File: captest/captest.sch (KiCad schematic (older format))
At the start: 12 parts, among them IC1 ATTINY861-P, P1 CONN_2, P2 CONN_6, P3 CONN_3X2

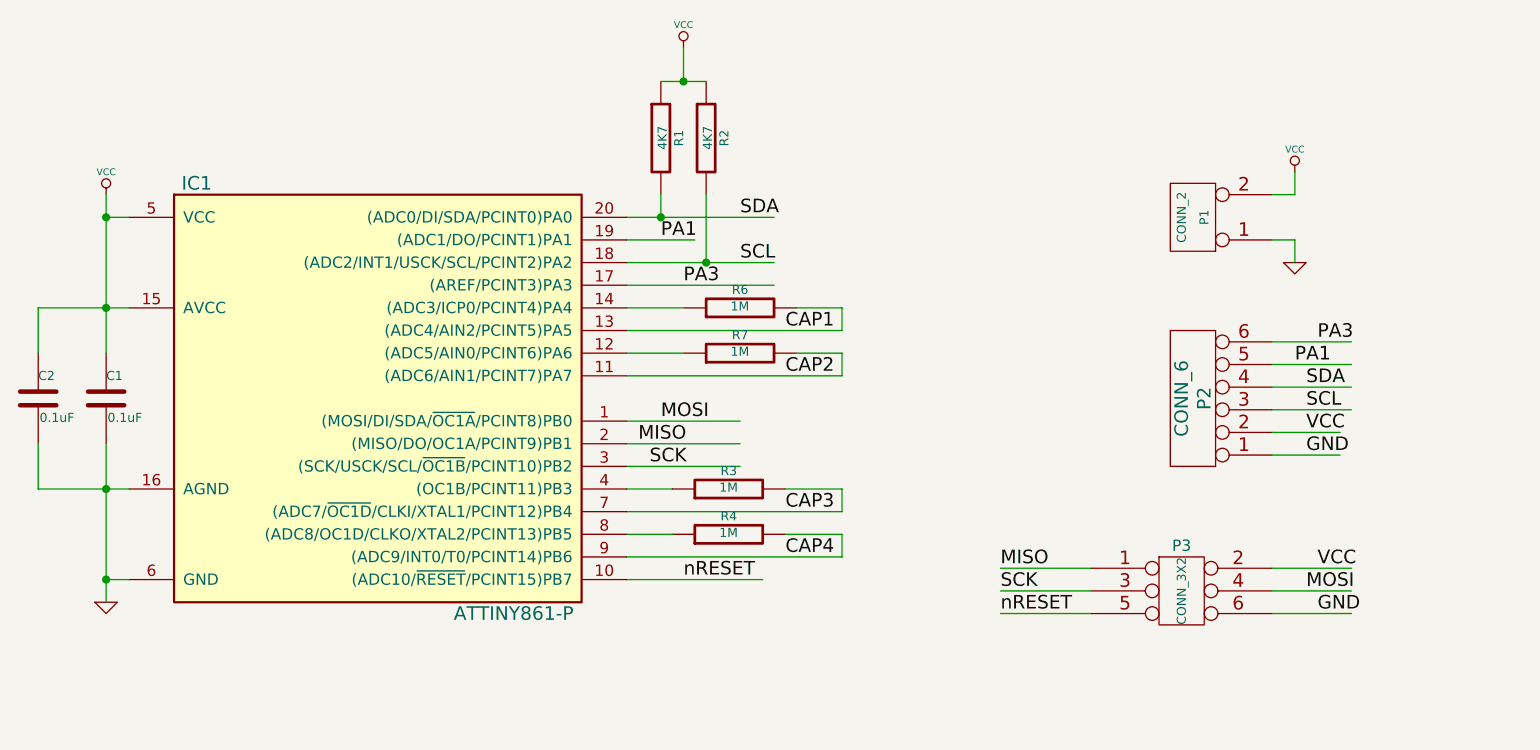
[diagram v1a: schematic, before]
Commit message: Captest updates
* Change to SOIC-20 version of ATtiny861
* Add filtering caps on sense pins
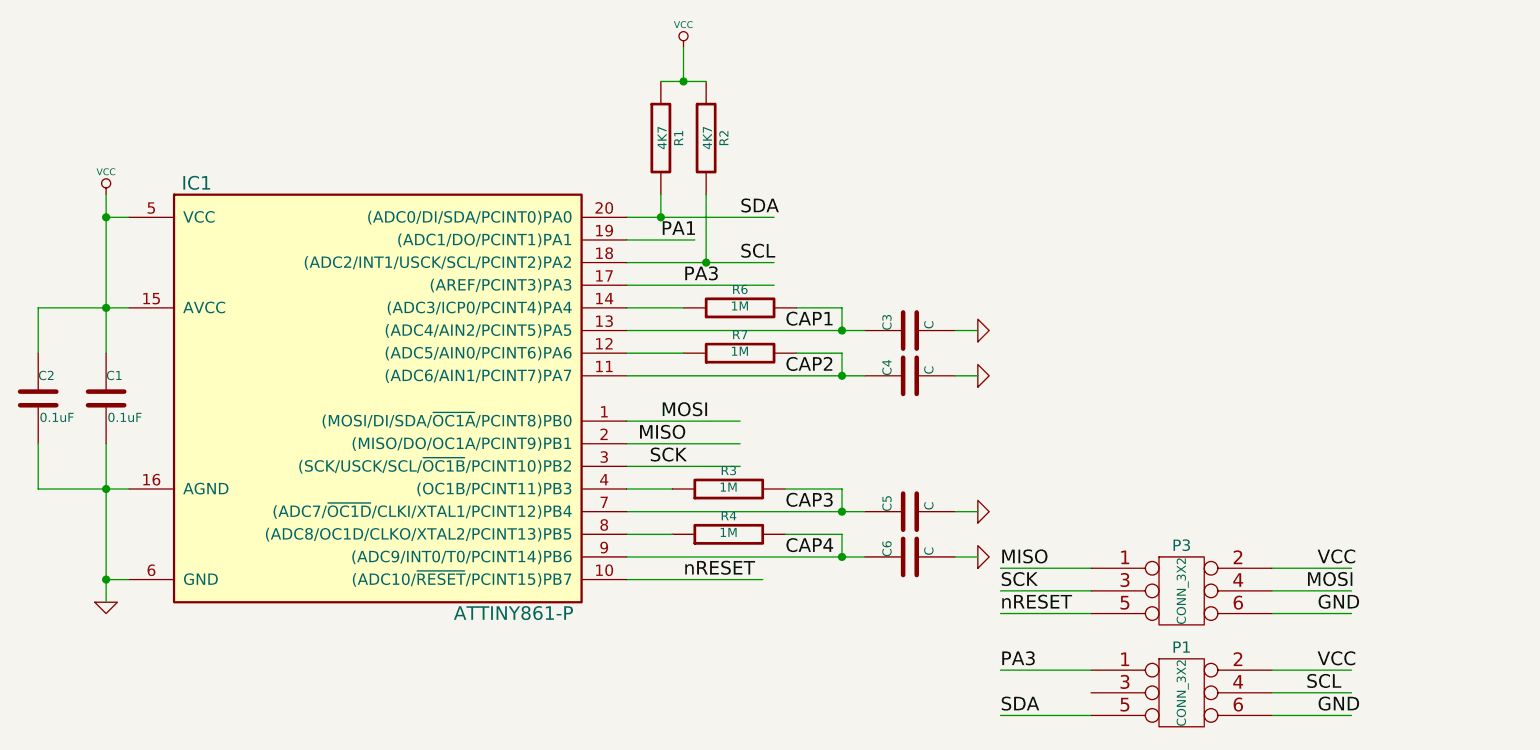
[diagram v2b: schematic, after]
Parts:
- removed P1: CONN_2, symbol CONN_2
- removed P2: CONN_6, symbol CONN_6
- added C3, C4, C5, C6: C, ~, symbol C
- added P1: CONN_3X2, symbol CONN_3X2
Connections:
- wire segments 52 -> 51
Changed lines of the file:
@@
-EESchema Schematic File Version 2  date Mon 04 Mar 2013 04:06:09 PM EST
+EESchema Schematic File Version 2  date Mon 04 Mar 2013 06:34:23 PM EST
 LIBS:power
 LIBS:device
@@
 	6800 2500 7050 2500
 Wire Wire Line
-	6800 2600 7750 2600
+	6800 2600 7850 2600
 Wire Wire Line
 	7750 2600 7750 2500
@@
 	6800 2700 7050 2700
 Wire Wire Line
-	6800 2800 7750 2800
+	6800 2800 7850 2800
 Wire Wire Line
 	7750 2800 7750 2700
@@
 Connection ~ 7050 1500
 Wire Wire Line
-	6800 3600 7750 3600
+	6800 3600 7850 3600
 Wire Wire Line
 	6800 3700 7400 3700
 Text Label 7050 3700 0    60   ~ 0
 nRESET
-$Comp
-L CONN_2 P1
-U 1 1 512E7DD4
-P 9300 2100
-F 0 "P1" V 9250 2100 40  0000 C CNN
-F 1 "CONN_2" V 9350 2100 40  0000 C CNN
-F 2 "" H 9300 2100 60  0000 C CNN
-F 3 "" H 9300 2100 60  0000 C CNN
-	1    9300 2100
-	-1   0    0    1
-$EndComp
-$Comp
-L GND #PWR03
-U 1 1 512E7DED
-P 9750 2300
-F 0 "#PWR03" H 9750 2300 30  0001 C CNN
-F 1 "GND" H 9750 2230 30  0001 C CNN
-F 2 "" H 9750 2300 60  0000 C CNN
-F 3 "" H 9750 2300 60  0000 C CNN
-	1    9750 2300
-	1    0    0    -1
-$EndComp
-Wire Wire Line
-	9650 2200 9750 2200
-Wire Wire Line
-	9750 2200 9750 2300
-$Comp
-L VCC #PWR04
-U 1 1 512E7E27
-P 9750 1900
-F 0 "#PWR04" H 9750 2000 30  0001 C CNN
-F 1 "VCC" H 9750 2000 30  0000 C CNN
-F 2 "" H 9750 1900 60  0000 C CNN
-F 3 "" H 9750 1900 60  0000 C CNN
-	1    9750 1900
-	1    0    0    -1
-$EndComp
-Wire Wire Line
-	9650 2000 9750 2000
-Wire Wire Line
-	9750 2000 9750 1900
-Wire Wire Line
-	9650 2950 10000 2950
-Text Label 9800 2950 0    60   ~ 0
-SCL
-Wire Wire Line
-	9650 2850 10000 2850
-Text Label 9800 2850 0    60   ~ 0
-SDA
 Wire Wire Line
 	6800 2200 7100 2200
 Text Label 6950 2200 0    60   ~ 0
 PA1
-$Comp
-L CONN_6 P2
-U 1 1 512E8037
-P 9300 2900
-F 0 "P2" V 9250 2900 60  0000 C CNN
-F 1 "CONN_6" V 9350 2900 60  0000 C CNN
-F 2 "" H 9300 2900 60  0000 C CNN
-F 3 "" H 9300 2900 60  0000 C CNN
-	1    9300 2900
-	-1   0    0    1
-$EndComp
-Wire Wire Line
-	9650 2650 10000 2650
-Text Label 9850 2650 0    60   ~ 0
-PA3
-Wire Wire Line
-	9650 3050 9950 3050
-Text Label 9800 3050 0    60   ~ 0
-VCC
-Wire Wire Line
-	9650 3150 9950 3150
-Text Label 9800 3150 0    60   ~ 0
-GND
 $Comp
 L ATTINY861-P IC1
@@
 	6800 3200 7300 3200
 Wire Wire Line
-	9650 2750 10000 2750
-Wire Wire Line
 	6800 2400 7450 2400
-Text Label 9750 2750 0    60   ~ 0
-PA1
 $Comp
 L R R3
@@
 	6800 3500 7000 3500
 Wire Wire Line
-	6800 3400 7750 3400
+	6800 3400 7850 3400
 Wire Wire Line
 	7750 3400 7750 3300
@@
 PA3
 $Comp
-L VCC #PWR05
+L VCC #PWR03
 U 1 1 513508A4
 P 4500 2000
-F 0 "#PWR05" H 4500 2100 30  0001 C CNN
+F 0 "#PWR03" H 4500 2100 30  0001 C CNN
 F 1 "VCC" H 4500 2100 30  0000 C CNN
 F 2 "" H 4500 2000 60  0000 C CNN
@@
 $EndComp
 Connection ~ 4500 2100
+$Comp
+L C C3
+U 1 1 51352673
+P 8050 2600
+F 0 "C3" H 8050 2700 40  0000 L CNN
+F 1 "C" H 8056 2515 40  0000 L CNN
+F 2 "~" H 8088 2450 30  0000 C CNN
+F 3 "~" H 8050 2600 60  0000 C CNN
+	1    8050 2600
+	0    -1   -1   0
+$EndComp
+$Comp
+L C C4
+U 1 1 51352682
+P 8050 2800
+F 0 "C4" H 8050 2900 40  0000 L CNN
+F 1 "C" H 8056 2715 40  0000 L CNN
+F 2 "~" H 8088 2650 30  0000 C CNN
+F 3 "~" H 8050 2800 60  0000 C CNN
+	1    8050 2800
+	0    -1   -1   0
+$EndComp
+Connection ~ 7750 2600
+Connection ~ 7750 2800
+$Comp
+L GND #PWR04
+U 1 1 5135270A
+P 8350 2600
+F 0 "#PWR04" H 8350 2600 30  0001 C CNN
+F 1 "GND" H 8350 2530 30  0001 C CNN
+F 2 "" H 8350 2600 60  0000 C CNN
+F 3 "" H 8350 2600 60  0000 C CNN
+	1    8350 2600
+	0    -1   -1   0
+$EndComp
+Wire Wire Line
+	8350 2600 8250 2600
+Wire Wire Line
+	8250 2800 8350 2800
+$Comp
+L GND #PWR05
+U 1 1 51352797
+P 8350 2800
+F 0 "#PWR05" H 8350 2800 30  0001 C CNN
+F 1 "GND" H 8350 2730 30  0001 C CNN
+F 2 "" H 8350 2800 60  0000 C CNN
+F 3 "" H 8350 2800 60  0000 C CNN
+	1    8350 2800
+	0    -1   -1   0
+$EndComp
+$Comp
+L C C5
+U 1 1 51352823
+P 8050 3400
+F 0 "C5" H 8050 3500 40  0000 L CNN
+F 1 "C" H 8056 3315 40  0000 L CNN
+F 2 "~" H 8088 3250 30  0000 C CNN
+F 3 "~" H 8050 3400 60  0000 C CNN
+	1    8050 3400
+	0    -1   -1   0
+$EndComp
+Connection ~ 7750 3400
+$Comp
+L GND #PWR06
+U 1 1 513528B2
+P 8350 3400
+F 0 "#PWR06" H 8350 3400 30  0001 C CNN
+F 1 "GND" H 8350 3330 30  0001 C CNN
+F 2 "" H 8350 3400 60  0000 C CNN
+F 3 "" H 8350 3400 60  0000 C CNN
+	1    8350 3400
+	0    -1   -1   0
+$EndComp
+Wire Wire Line
+	8350 3400 8250 3400
+$Comp
+L C C6
+U 1 1 51352902
+P 8050 3600
+F 0 "C6" H 8050 3700 40  0000 L CNN
+F 1 "C" H 8056 3515 40  0000 L CNN
+F 2 "~" H 8088 3450 30  0000 C CNN
+F 3 "~" H 8050 3600 60  0000 C CNN
+	1    8050 3600
+	0    -1   -1   0
+$EndComp
+Connection ~ 7750 3600
+$Comp
+L GND #PWR07
+U 1 1 51352953
+P 8350 3600
+F 0 "#PWR07" H 8350 3600 30  0001 C CNN
+F 1 "GND" H 8350 3530 30  0001 C CNN
+F 2 "" H 8350 3600 60  0000 C CNN
+F 3 "" H 8350 3600 60  0000 C CNN
+	1    8350 3600
+	0    -1   -1   0
+$EndComp
+Wire Wire Line
+	8350 3600 8250 3600
+$Comp
+L CONN_3X2 P1
+U 1 1 513529F0
+P 9250 4250
+F 0 "P1" H 9250 4500 50  0000 C CNN
+F 1 "CONN_3X2" V 9250 4300 40  0000 C CNN
+F 2 "" H 9250 4250 60  0000 C CNN
+F 3 "" H 9250 4250 60  0000 C CNN
+	1    9250 4250
+	1    0    0    -1
+$EndComp
+Wire Wire Line
+	9650 4100 10000 4100
+Wire Wire Line
+	9650 4200 10000 4200
+Wire Wire Line
+	9650 4300 10000 4300
+Wire Wire Line
+	8450 4100 8850 4100
+Wire Wire Line
+	8450 4300 8850 4300
+Text Label 9850 4100 0    60   ~ 0
+VCC
+Text Label 9800 4200 0    60   ~ 0
+SCL
+Text Label 9850 4300 0    60   ~ 0
+GND
+Text Label 8450 4100 0    60   ~ 0
+PA3
+Text Label 8450 4300 0    60   ~ 0
+SDA
 $EndSCHEMATC

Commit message: Captest update with TSSOP and more density
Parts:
- removed P3: CONN_3X2, symbol CONN_3X2
- added L1: INDUCTOR, ~, symbol INDUCTOR
- added P2: CONN_4, symbol CONN_4
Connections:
- net labels added: PWR
- net labels removed: PA1
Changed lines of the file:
@@
-EESchema Schematic File Version 2  date Mon 04 Mar 2013 06:34:23 PM EST
+EESchema Schematic File Version 2  date Tue 05 Mar 2013 12:00:50 PM EST
 LIBS:power
 LIBS:device
@@
 Sheet 1 1
 Title ""
-Date "4 mar 2013"
+Date "5 mar 2013"
 Rev ""
 Comp ""
@@
 	0    -1   -1   0
 $EndComp
-Wire Wire Line
-	6800 2500 7050 2500
-Wire Wire Line
-	6800 2600 7850 2600
-Wire Wire Line
-	7750 2600 7750 2500
-Wire Wire Line
-	7750 2500 7550 2500
-Wire Wire Line
-	6800 2700 7050 2700
-Wire Wire Line
-	6800 2800 7850 2800
-Wire Wire Line
-	7750 2800 7750 2700
-Wire Wire Line
-	7750 2700 7550 2700
 Text Label 7500 2800 0    60   ~ 0
 CAP2
 Text Label 7500 2600 0    60   ~ 0
 CAP1
-Wire Wire Line
-	6800 2100 7450 2100
-Wire Wire Line
-	6800 2300 7450 2300
 Text Label 7300 2300 0    60   ~ 0
 SCL
 Text Label 7300 2100 0    60   ~ 0
 SDA
-Wire Wire Line
-	4600 2100 4500 2100
-Wire Wire Line
-	4500 2000 4500 2700
-Wire Wire Line
-	4200 2500 4600 2500
 $Comp
 L GND #PWR01
@@
 	1    0    0    -1
 $EndComp
-Wire Wire Line
-	4500 3100 4500 3800
-Wire Wire Line
-	4500 3700 4600 3700
-Wire Wire Line
-	4200 3300 4600 3300
-Connection ~ 4500 3700
 $Comp
 L C C1
@@
 	1    0    0    -1
 $EndComp
-Connection ~ 4500 2500
-Connection ~ 4500 3300
 Text Label 6850 3100 0    60   ~ 0
 MISO
-Wire Wire Line
-	6800 3000 7300 3000
 Text Label 6950 3000 0    60   ~ 0
 MOSI
@@
 	1    0    0    -1
 $EndComp
-Wire Wire Line
-	7150 2000 7150 2300
-Connection ~ 7150 2300
-Wire Wire Line
-	6950 2000 6950 2100
-Connection ~ 6950 2100
 $Comp
 L VCC #PWR02
@@
 	1    0    0    -1
 $EndComp
-Wire Wire Line
-	6950 1500 7150 1500
-Wire Wire Line
-	7050 1500 7050 1350
-Connection ~ 7050 1500
-Wire Wire Line
-	6800 3600 7850 3600
-Wire Wire Line
-	6800 3700 7400 3700
 Text Label 7050 3700 0    60   ~ 0
 nRESET
-Wire Wire Line
-	6800 2200 7100 2200
-Text Label 6950 2200 0    60   ~ 0
-PA1
 $Comp
 L ATTINY861-P IC1
@@
 	1    0    0    -1
 $EndComp
-Wire Wire Line
-	6800 3100 7300 3100
-Wire Wire Line
-	6800 3200 7300 3200
-Wire Wire Line
-	6800 2400 7450 2400
 $Comp
 L R R3
@@
 	0    -1   -1   0
 $EndComp
-Wire Wire Line
-	6800 3300 7000 3300
 $Comp
 L R R4
@@
 	0    -1   -1   0
 $EndComp
-Wire Wire Line
-	6800 3500 7000 3500
-Wire Wire Line
-	6800 3400 7850 3400
-Wire Wire Line
-	7750 3400 7750 3300
-Wire Wire Line
-	7750 3300 7500 3300
-Wire Wire Line
-	7750 3600 7750 3500
-Wire Wire Line
-	7750 3500 7500 3500
 Text Label 7500 3400 0    60   ~ 0
 CAP3
 Text Label 7500 3600 0    60   ~ 0
 CAP4
-$Comp
-L CONN_3X2 P3
-U 1 1 5135027D
-P 9250 3800
-F 0 "P3" H 9250 4050 50  0000 C CNN
-F 1 "CONN_3X2" V 9250 3850 40  0000 C CNN
-F 2 "" H 9250 3800 60  0000 C CNN
-F 3 "" H 9250 3800 60  0000 C CNN
-	1    9250 3800
-	1    0    0    -1
-$EndComp
-Wire Wire Line
-	9650 3650 10000 3650
-Wire Wire Line
-	9650 3750 10000 3750
-Wire Wire Line
-	9650 3850 10000 3850
-Wire Wire Line
-	8450 3650 8850 3650
-Wire Wire Line
-	8450 3750 8850 3750
-Wire Wire Line
-	8450 3850 8850 3850
-Text Label 9850 3650 0    60   ~ 0
-VCC
-Text Label 9800 3750 0    60   ~ 0
-MOSI
-Text Label 9850 3850 0    60   ~ 0
-GND
 Text Label 8450 3650 0    60   ~ 0
 MISO
@@
 	1    0    0    -1
 $EndComp
-Wire Wire Line
-	4200 2700 4200 2500
-Wire Wire Line
-	4200 3100 4200 3300
 Text Label 7050 2400 0    60   ~ 0
 PA3
@@
 	1    0    0    -1
 $EndComp
-Connection ~ 4500 2100
 $Comp
 L C C3
@@
 	0    -1   -1   0
 $EndComp
-Connection ~ 7750 2600
-Connection ~ 7750 2800
 $Comp
 L GND #PWR04
@@
 	0    -1   -1   0
 $EndComp
-Wire Wire Line
-	8350 2600 8250 2600
-Wire Wire Line
-	8250 2800 8350 2800
 $Comp
 L GND #PWR05
@@
 	0    -1   -1   0
 $EndComp
-Connection ~ 7750 3400
 $Comp
 L GND #PWR06
@@
 	0    -1   -1   0
 $EndComp
-Wire Wire Line
-	8350 3400 8250 3400
 $Comp
 L C C6
@@
 	0    -1   -1   0
 $EndComp
-Connection ~ 7750 3600
 $Comp
 L GND #PWR07
@@
 	0    -1   -1   0
 $EndComp
-Wire Wire Line
-	8350 3600 8250 3600
 $Comp
 L CONN_3X2 P1
@@
 	1    0    0    -1
 $EndComp
-Wire Wire Line
-	9650 4100 10000 4100
-Wire Wire Line
-	9650 4200 10000 4200
-Wire Wire Line
-	9650 4300 10000 4300
-Wire Wire Line
-	8450 4100 8850 4100
-Wire Wire Line
-	8450 4300 8850 4300
-Text Label 9850 4100 0    60   ~ 0
-VCC
-Text Label 9800 4200 0    60   ~ 0
-SCL
 Text Label 9850 4300 0    60   ~ 0
 GND
 Text Label 8450 4100 0    60   ~ 0
+SDA
+Text Label 8450 4300 0    60   ~ 0
 PA3
-Text Label 8450 4300 0    60   ~ 0
+$Comp
+L INDUCTOR L1
+U 1 1 5136118C
+P 10300 4100
+F 0 "L1" V 10250 4100 40  0000 C CNN
+F 1 "INDUCTOR" V 10400 4100 40  0000 C CNN
+F 2 "~" H 10300 4100 60  0000 C CNN
+F 3 "~" H 10300 4100 60  0000 C CNN
+	1    10300 4100
+	0    -1   -1   0
+$EndComp
+Wire Wire Line
+	6800 2500 7050 2500
+Wire Wire Line
+	6800 2600 7850 2600
+Wire Wire Line
+	7750 2600 7750 2500
+Wire Wire Line
+	7750 2500 7550 2500
+Wire Wire Line
+	6800 2700 7050 2700
+Wire Wire Line
+	6800 2800 7850 2800
+Wire Wire Line
+	7750 2800 7750 2700
+Wire Wire Line
+	7750 2700 7550 2700
+Wire Wire Line
+	6800 2100 7450 2100
+Wire Wire Line
+	6800 2300 7450 2300
+Wire Wire Line
+	4600 2100 4500 2100
+Wire Wire Line
+	4500 2000 4500 2700
+Wire Wire Line
+	4200 2500 4600 2500
+Wire Wire Line
+	4500 3100 4500 3800
+Wire Wire Line
+	4500 3700 4600 3700
+Wire Wire Line
+	4200 3300 4600 3300
+Connection ~ 4500 3700
+Connection ~ 4500 2500
+Connection ~ 4500 3300
+Wire Wire Line
+	6800 3000 7300 3000
+Wire Wire Line
+	7150 2000 7150 2300
+Connection ~ 7150 2300
+Wire Wire Line
+	6950 2000 6950 2100
+Connection ~ 6950 2100
+Wire Wire Line
+	6950 1500 7150 1500
+Wire Wire Line
+	7050 1500 7050 1350
+Connection ~ 7050 1500
+Wire Wire Line
+	6800 3600 7850 3600
+Wire Wire Line
+	6800 3700 7400 3700
+Wire Wire Line
+	6800 3100 7300 3100
+Wire Wire Line
+	6800 3200 7300 3200
+Wire Wire Line
+	6800 2400 7450 2400
+Wire Wire Line
+	6800 3300 7000 3300
+Wire Wire Line
+	6800 3500 7000 3500
+Wire Wire Line
+	6800 3400 7850 3400
+Wire Wire Line
+	7750 3400 7750 3300
+Wire Wire Line
+	7750 3300 7500 3300
+Wire Wire Line
+	7750 3600 7750 3500
+Wire Wire Line
+	7750 3500 7500 3500
+Wire Wire Line
+	8450 3650 8850 3650
+Wire Wire Line
+	8450 3750 8850 3750
+Wire Wire Line
+	8450 3850 8850 3850
+Wire Wire Line
+	4200 2700 4200 2500
+Wire Wire Line
+	4200 3100 4200 3300
+Connection ~ 4500 2100
+Connection ~ 7750 2600
+Connection ~ 7750 2800
+Wire Wire Line
+	8350 2600 8250 2600
+Wire Wire Line
+	8250 2800 8350 2800
+Connection ~ 7750 3400
+Wire Wire Line
+	8350 3400 8250 3400
+Connection ~ 7750 3600
+Wire Wire Line
+	8350 3600 8250 3600
+Wire Wire Line
+	9650 4100 10000 4100
+Wire Wire Line
+	9650 4200 10000 4200
+Wire Wire Line
+	9650 4300 10000 4300
+Wire Wire Line
+	8450 4100 8850 4100
+Wire Wire Line
+	8450 4300 8850 4300
+$Comp
+L VCC #PWR08
+U 1 1 51361A88
+P 10700 4000
+F 0 "#PWR08" H 10700 4100 30  0001 C CNN
+F 1 "VCC" H 10700 4100 30  0000 C CNN
+F 2 "" H 10700 4000 60  0000 C CNN
+F 3 "" H 10700 4000 60  0000 C CNN
+	1    10700 4000
+	1    0    0    -1
+$EndComp
+Wire Wire Line
+	10700 4000 10700 4100
+Wire Wire Line
+	10700 4100 10600 4100
+$Comp
+L CONN_4 P2
+U 1 1 51361ADF
+P 9200 3700
+F 0 "P2" V 9150 3700 50  0000 C CNN
+F 1 "CONN_4" V 9250 3700 50  0000 C CNN
+F 2 "" H 9200 3700 60  0000 C CNN
+F 3 "" H 9200 3700 60  0000 C CNN
+	1    9200 3700
+	1    0    0    -1
+$EndComp
+Wire Wire Line
+	8850 3550 8450 3550
+Text Label 8450 3550 0    60   ~ 0
+MOSI
+Wire Wire Line
+	8450 4200 8850 4200
+Text Label 8450 4200 0    60   ~ 0
+SCL
+Text Label 9700 4200 0    60   ~ 0
 SDA
+Text Label 9750 4100 0    60   ~ 0
+PWR
 $EndSCHEMATC

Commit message: Optimize captest layout
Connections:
- wire segments 51 -> 52
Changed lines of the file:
@@
-EESchema Schematic File Version 2  date Tue 05 Mar 2013 12:00:50 PM EST
+EESchema Schematic File Version 2  date Tue 05 Mar 2013 12:08:52 PM EST
 LIBS:power
 LIBS:device
@@
 Text Label 9750 4100 0    60   ~ 0
 PWR
+$Comp
+L GND #PWR?
+U 1 1 5136274D
+P 7000 2200
+F 0 "#PWR?" H 7000 2200 30  0001 C CNN
+F 1 "GND" H 7000 2130 30  0001 C CNN
+F 2 "" H 7000 2200 60  0000 C CNN
+F 3 "" H 7000 2200 60  0000 C CNN
+	1    7000 2200
+	0    -1   -1   0
+$EndComp
+Wire Wire Line
+	7000 2200 6800 2200
 $EndSCHEMATC
